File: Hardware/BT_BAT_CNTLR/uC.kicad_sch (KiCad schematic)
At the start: 0 parts

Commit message: dead ass think I just added a second copy..
aight. routed caps and antenna for nRF.
need to route power and find a new IC for USB ports.
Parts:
- added AE1: Antenna_Chip, RF_Antenna:Texas_SWRA117D_2.4GHz_Right, symbol Device:Antenna_Chip
- added C10, C13: 4.7uF, Capacitor_SMD:C_0603_1608Metric, symbol Device:C
- added C11, C12: 100nF, Capacitor_SMD:C_0603_1608Metric, symbol Device:C
- added C14: 01.uF, Capacitor_SMD:C_0603_1608Metric, symbol Device:C
- added C15: 100pF, Capacitor_SMD:C_0603_1608Metric, symbol Device:C
- added C16: 1uF, Capacitor_SMD:C_0603_1608Metric, symbol Device:C
- added C17: 820pF, Capacitor_SMD:C_0603_1608Metric, symbol Device:C
- added C7, C8: 20pF, Capacitor_SMD:C_0402_1005Metric, symbol Device:C_Small
- added C9: 1.0uF, Capacitor_SMD:C_0603_1608Metric, symbol Device:C
- added U3: nRF52820-QDxx, Package_DFN_QFN:QFN-40-1EP_5x5mm_P0.4mm_EP3.6x3.6mm, symbol MCU_Nordic:nRF52820-QDxx
- added Y1: Crystal_GND24, Oscillator:Oscillator_SMD_Kyocera_KC2520Z-4Pin_2.5x2.0mm, symbol Device:Crystal_GND24
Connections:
- new net: C16.2, U3.26 (DEC6), U3.38 (DEC4)
- new net: C15.2, U3.27 (DEC3)
- new net: C7.1, U3.28 (XC1), Y1.3
- new net: C8.1, U3.29 (XC2), Y1.1
- new net: C14.2, U3.1 (DEC1)
- new net: C17.2, U3.21 (DEC5)
- new net +3V3: C10.2, C11.2, C12.2, C13.2, C9.2, U3.18 (VDD), U3.30 (VDD), U3.40 (VDD), U3.8 (VDD), U3.9 (VDDH)
- new net ANT: AE1.2 (PCB_Trace), U3.24 (ANT)
- new net GND: AE1.1 (FEED), C10.1, C11.1, C12.1, C13.1, C14.1, C15.1, C16.1, C17.1, C7.2, C8.2, C9.1, U3.10 (VBUS), U3.25 (VSS_PA), U3.37 (VSS), U3.41 (VSS), Y1.2, Y1.4
- no-connect marks 0 -> 4

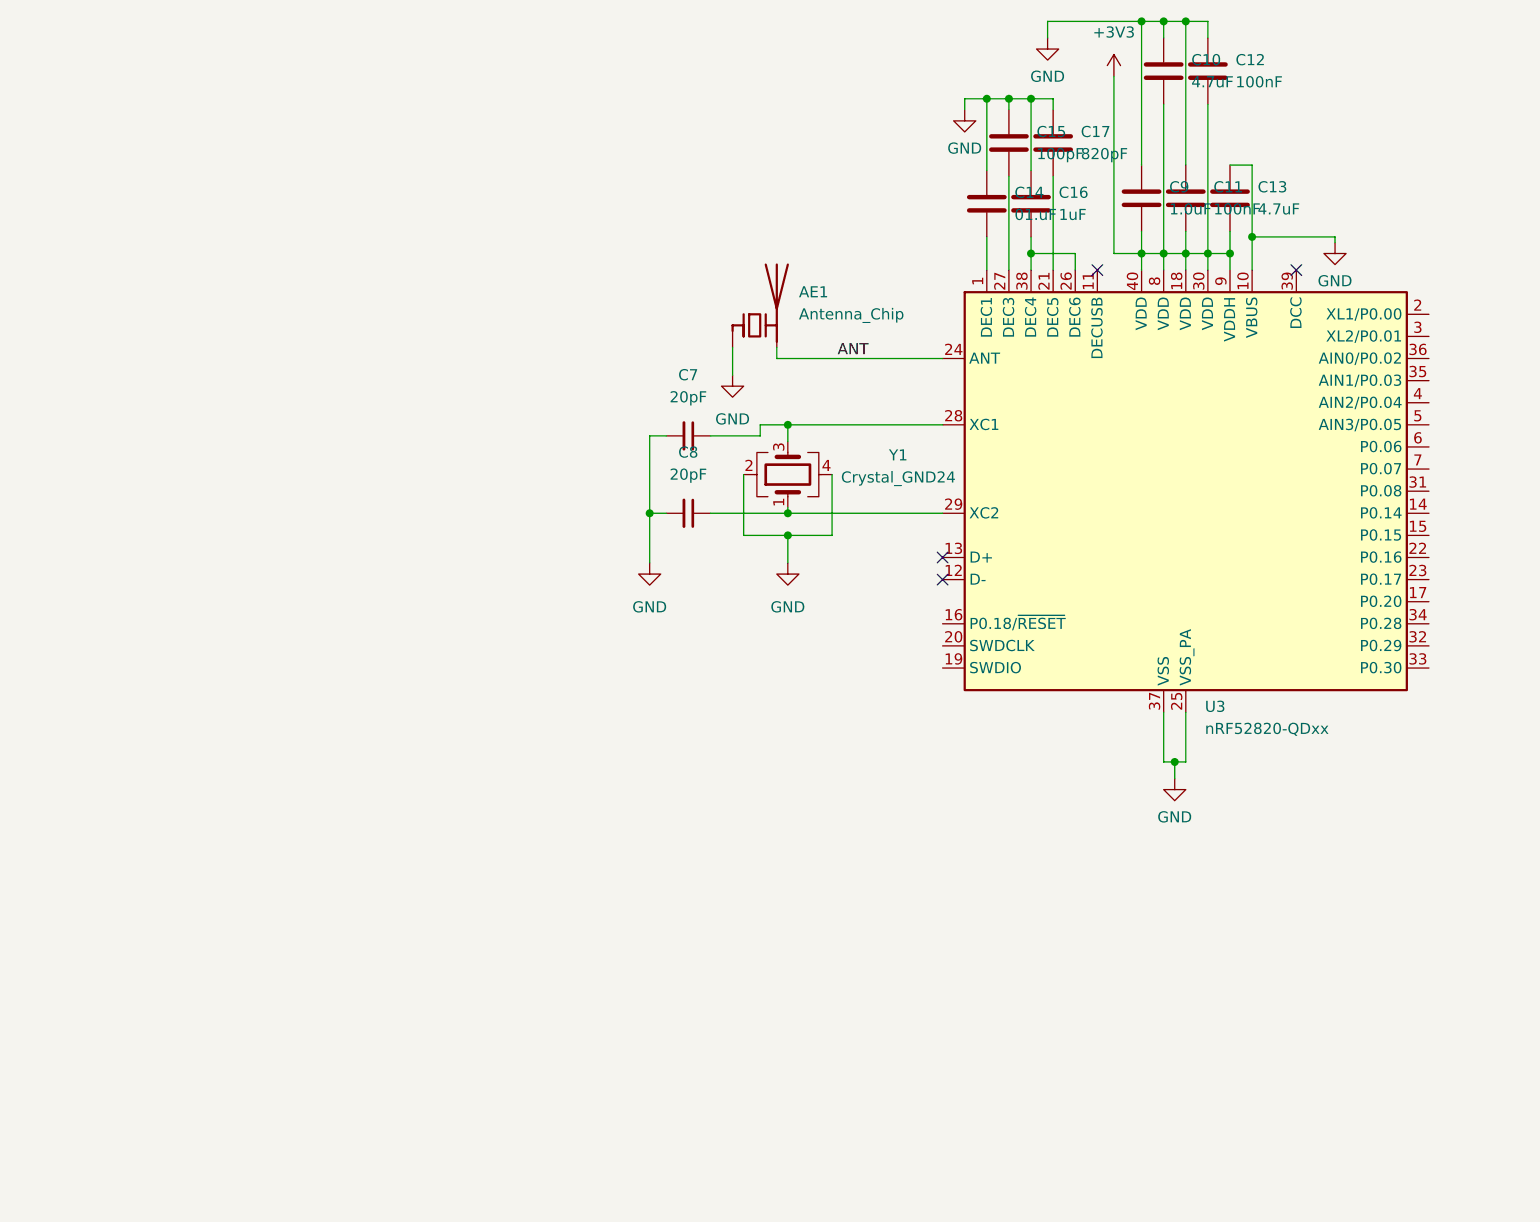
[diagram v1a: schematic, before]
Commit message: Added 1 USB circuit
will wait for approval/ review before continuing
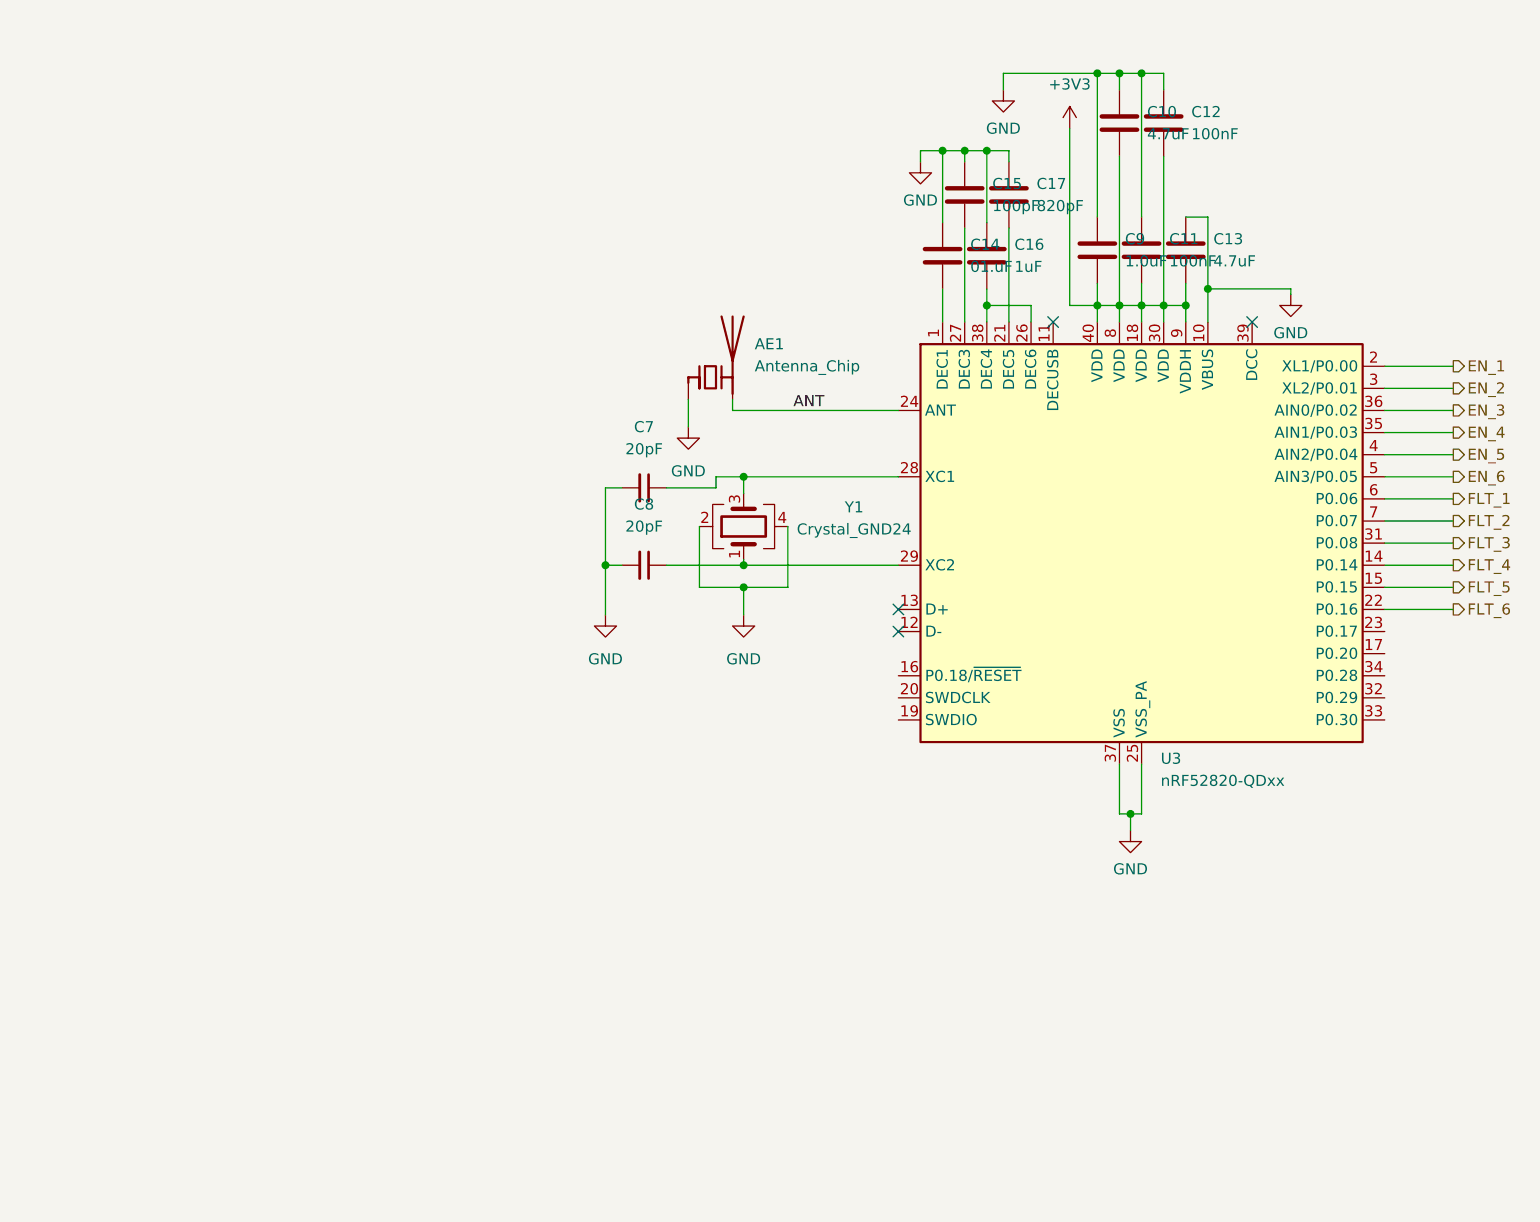
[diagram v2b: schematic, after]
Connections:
- net FLT_4: now reaches U3.14 (P0.14)
- net FLT_5: now reaches U3.15 (P0.15)
- net EN_1: now reaches U3.2 (XL1/P0.00)
- net FLT_6: now reaches U3.22 (P0.16)
- net EN_2: now reaches U3.3 (XL2/P0.01)
- net FLT_3: now reaches U3.31 (P0.08)
- net EN_4: now reaches U3.35 (AIN1/P0.03)
- net EN_3: now reaches U3.36 (AIN0/P0.02)
- net EN_5: now reaches U3.4 (AIN2/P0.04)
- net EN_6: now reaches U3.5 (AIN3/P0.05)
- net FLT_1: now reaches U3.6 (P0.06)
- net FLT_2: now reaches U3.7 (P0.07)
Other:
- moved on the sheet: AE1, C10, C11, C12, C13, C14, C15, C16, C17, C7, C8, C9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

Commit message: - Github Tree Cleanup - Power Routing
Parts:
- added J8: Conn_ARM_SWD_TagConnect_TC2030, Connector:Tag-Connect_TC2030-IDC-FP_2x03_P1.27mm_Vertical, symbol Connector:Conn_ARM_SWD_TagConnect_TC2030
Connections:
- net +3V3: now also J8.1 (VCC)
- net GND: now also J8.5 (GND)
- net RESET: now reaches U3.16 (P0.18/~{RESET})
- net RESET: now also J8.3 (~{RESET})
- net SWDIO: now reaches U3.19 (SWDIO)
- net SWDIO: now also J8.2 (SWDIO)
- net SWDCLK: now reaches U3.20 (SWDCLK)
- net SWDCLK: now also J8.4 (SWCLK)
- no-connect marks 4 -> 5
